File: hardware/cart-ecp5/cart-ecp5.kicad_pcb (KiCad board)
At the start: 4 copper layers, 100 x 60 mm, 129 parts, among them J1 JTAG, J2 MicroSD_Molex_1040310811, J3 N64_Cartridge_Bus, J5 USB_C_USB2.0, U1 LFE5U-25F-xBG256x, U10 93C46BT-I_OT, U11 FT2232HQ, U13 TLV62568DBV, U2 W25Q512JVEIM, U3 S27KS0641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

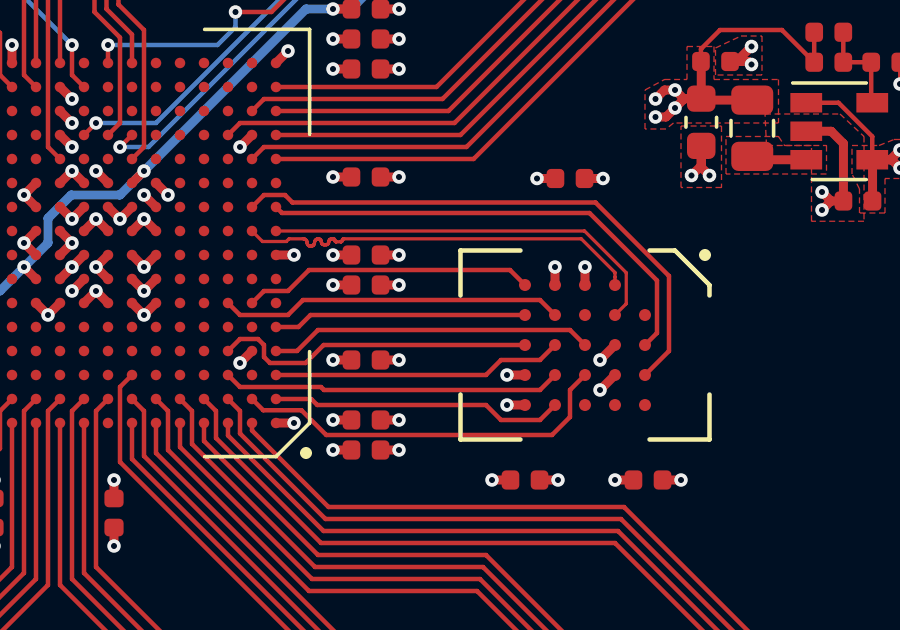
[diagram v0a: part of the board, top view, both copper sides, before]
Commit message: First pass at length matching HyperRAM interface
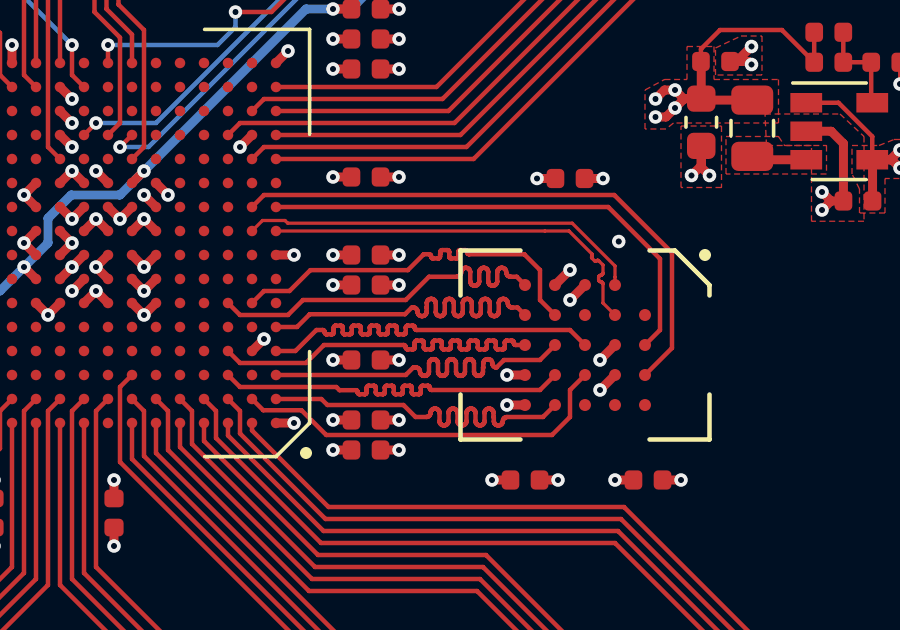
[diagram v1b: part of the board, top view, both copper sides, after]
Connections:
- U1 pad F2: HRAM_DQ7 -> HRAM_DQ1
- U1 pad F3: HRAM_DQ1 -> HRAM_DQ7
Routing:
- net HRAM_DQ6: track 8.47 -> 13.1 mm
- net HRAM_DQ0: track 9.71 -> 13.1 mm
- net HRAM_DQ4: track 9.80 -> 13.1 mm
- net HRAM_DQ7: track 9.76 -> 12.9 mm
- net HRAM_RWDS: track 10.8 -> 13.0 mm
- net HRAM_DQ5: track 10.9 -> 13.0 mm
- net HRAM_DQ3: track 11.3 -> 13.0 mm
- net HRAM_DQ1: track 11.5 -> 13.0 mm
- net HRAM_RESET_B: track 18.8 -> 19.4 mm
- net HRAM_CS_B: track 16.0 -> 16.6 mm
- net GND: track 187.9 -> 188.0 mm, vias 108 -> 109

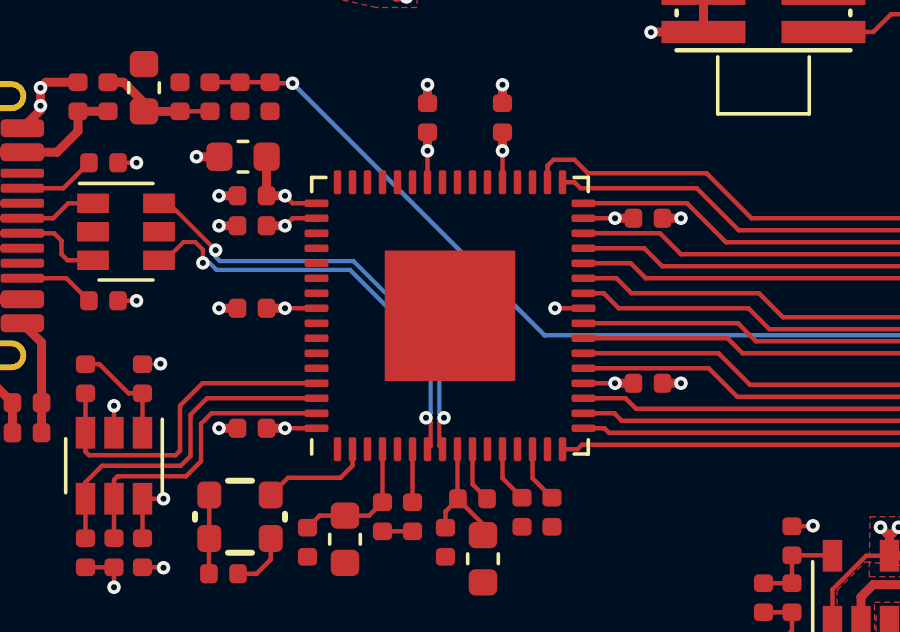
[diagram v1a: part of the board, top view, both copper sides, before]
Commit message: Adjust the P1V8 power plane to insect the switcher output
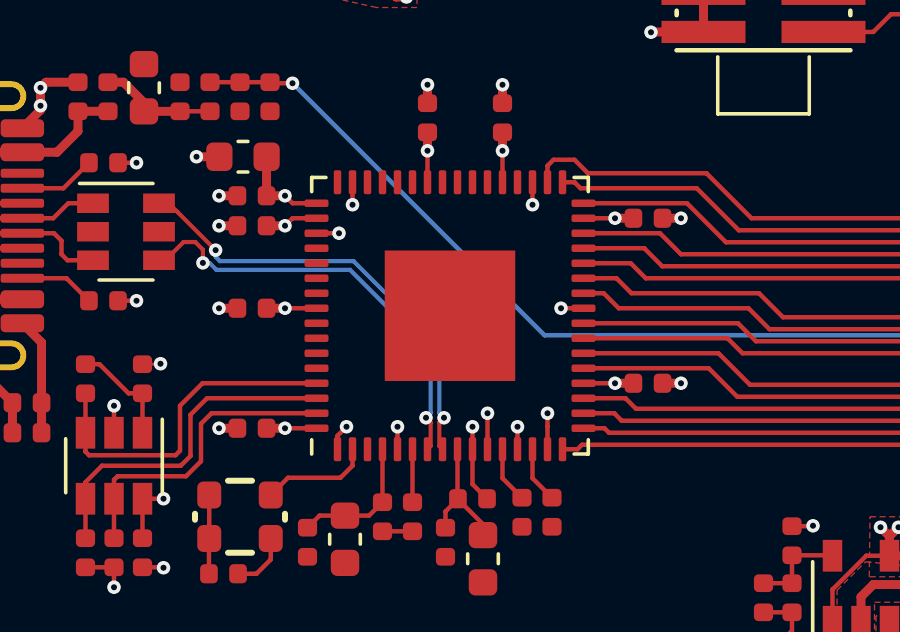
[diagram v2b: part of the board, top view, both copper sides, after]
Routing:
- net GND: track 188.0 -> 195.6 mm, vias 109 -> 118

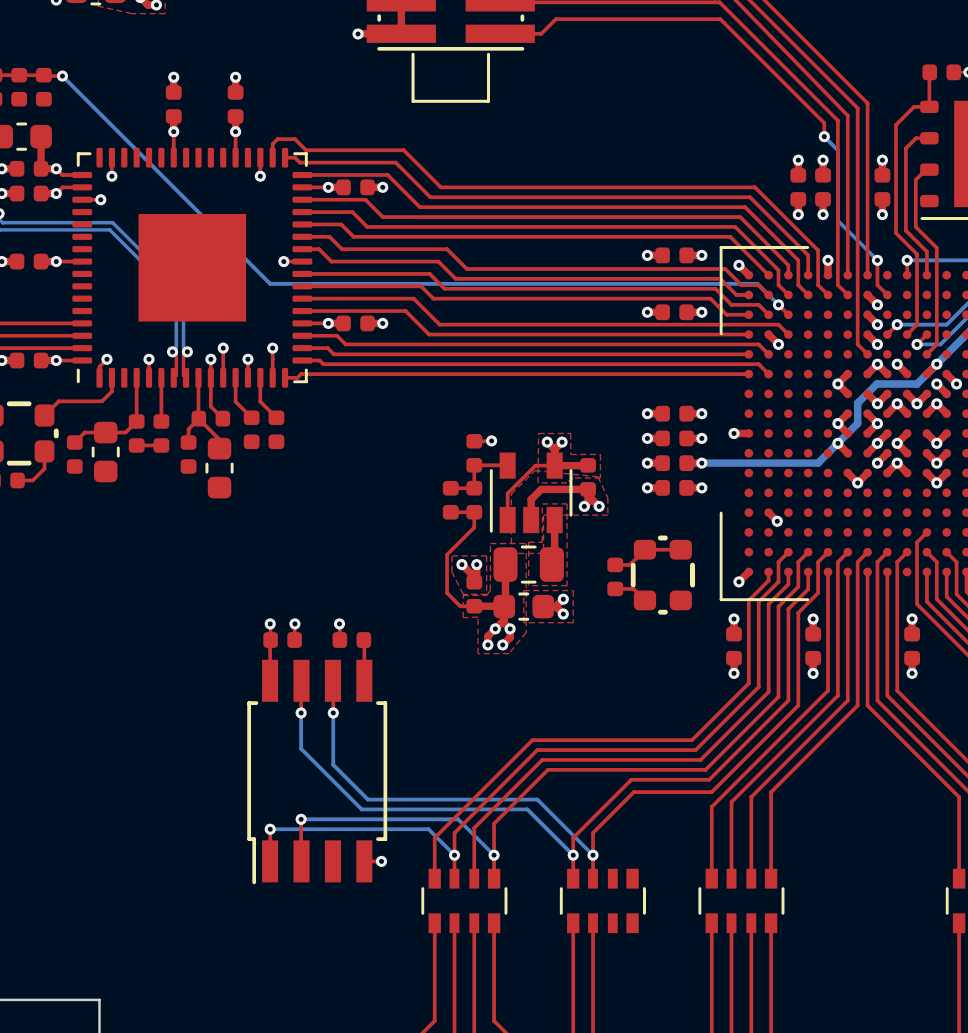
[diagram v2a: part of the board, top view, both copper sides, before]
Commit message: Add more clearance to FT2232H interface to study length matching
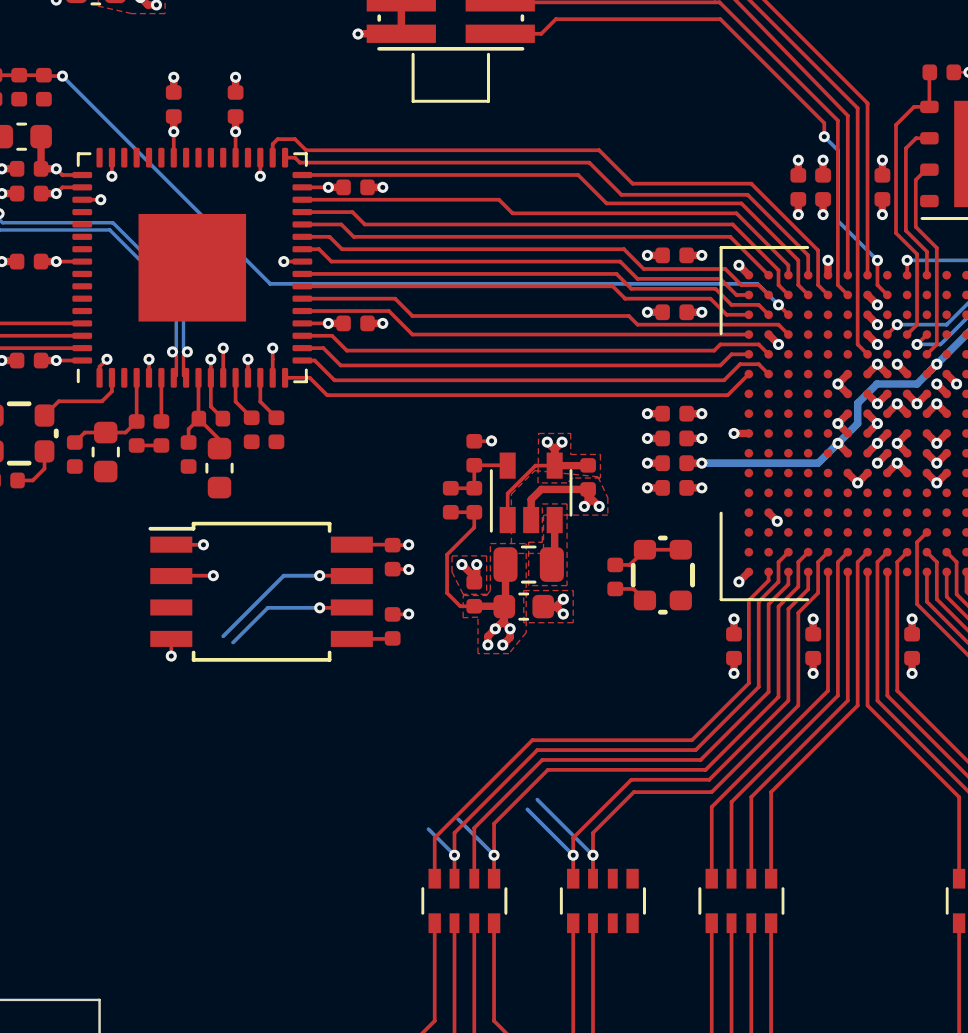
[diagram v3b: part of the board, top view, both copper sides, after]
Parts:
- moved U4 7.59 mm to (124.3, 107.0), turned to 0 degrees
- moved C41 5.57 mm to (129.6, 105.6), turned to 270 degrees
- moved R6 1.74 mm to (129.6, 108.4), turned to 270 degrees
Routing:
- net N64_CIC_DATA2: track 34.4 -> 27.5 mm
- net N64_CIC_DATA1: track 33.7 -> 27.0 mm
- net N64_COLD_RESET#: track 31.7 -> 25.3 mm
- net N64_S_CLK: track 32.3 -> 26.0 mm
- net USB_AD0: track 18.8 -> 19.4 mm
- net USB_AD1: track 19.1 -> 19.6 mm

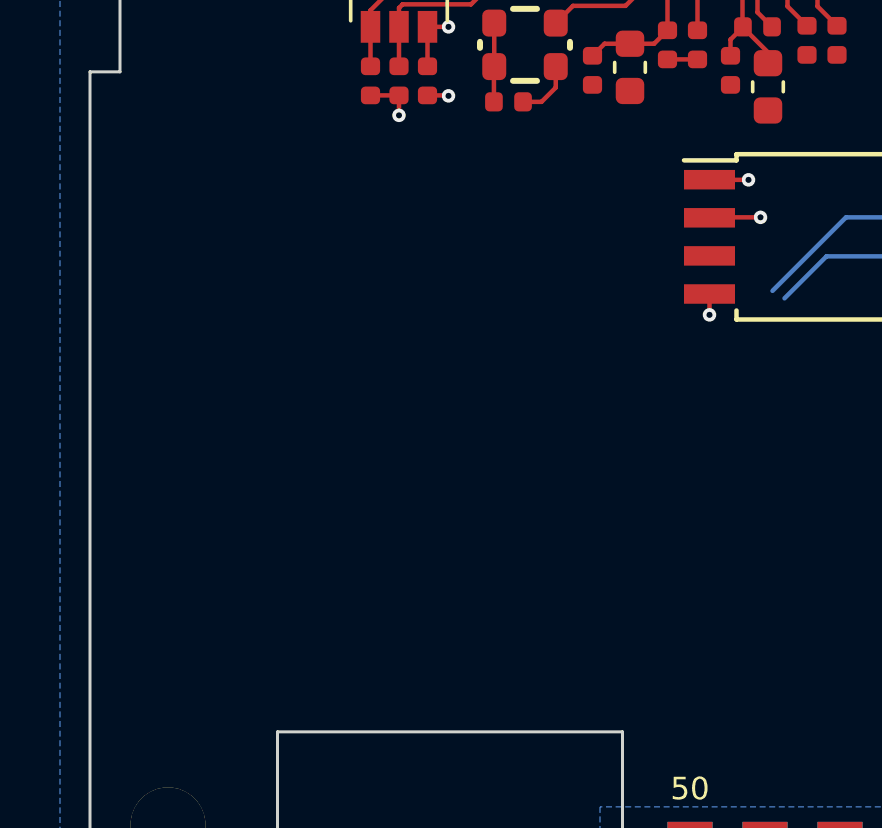
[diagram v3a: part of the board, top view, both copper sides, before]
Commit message: Add debugging LEDs with preliminary layout
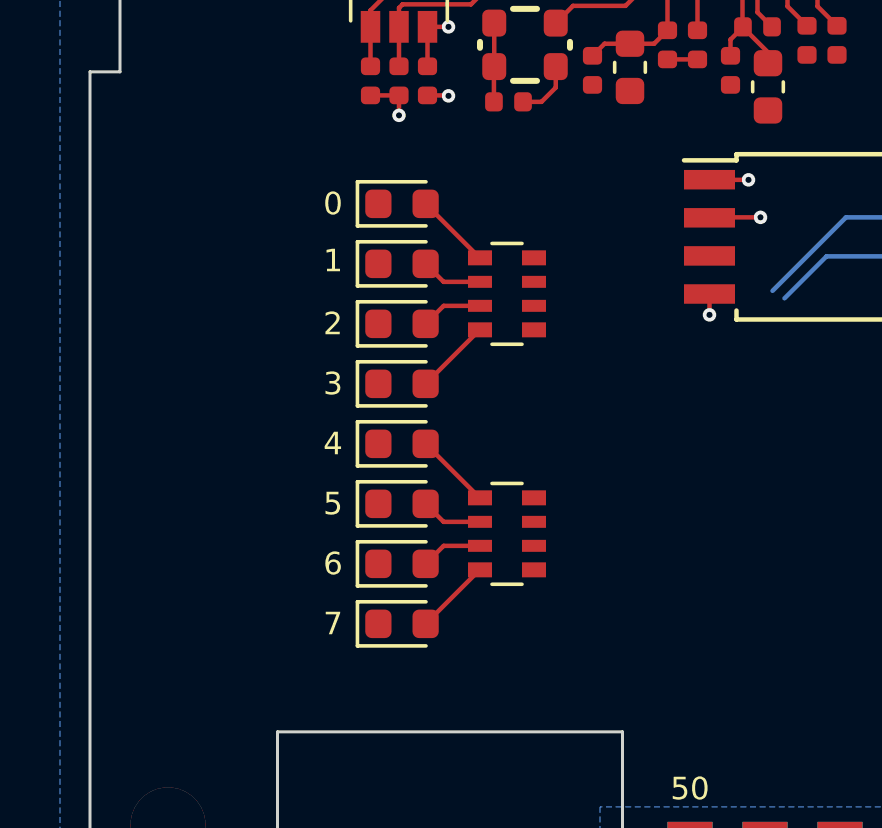
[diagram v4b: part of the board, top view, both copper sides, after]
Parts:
- added D1: LED, Diode_SMD:D_0603_1608Metric, F.Cu at (110.4, 105.9)
- added D2: LED, Diode_SMD:D_0603_1608Metric, F.Cu at (110.4, 107.9)
- added D3: LED, Diode_SMD:D_0603_1608Metric, F.Cu at (110.4, 109.9)
- added D4: LED, Diode_SMD:D_0603_1608Metric, F.Cu at (110.4, 111.9)
- added D5: LED, Diode_SMD:D_0603_1608Metric, F.Cu at (110.4, 113.9)
- added D6: LED, Diode_SMD:D_0603_1608Metric, F.Cu at (110.4, 115.9)
- added D7: LED, Diode_SMD:D_0603_1608Metric, F.Cu at (110.4, 117.9)
- added D8: LED, Diode_SMD:D_0603_1608Metric, F.Cu at (110.4, 119.9)
- added RN10: 200R, Resistor_SMD:R_Array_Convex_4x0603, F.Cu at (113.9, 116.9)
- added RN9: 200R, Resistor_SMD:R_Array_Convex_4x0603, F.Cu at (113.9, 108.9)
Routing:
- net Net-(D8-Pad2): track 0.00 -> 2.56 mm
- net Net-(D4-Pad2): track 0.00 -> 2.56 mm
- net Net-(D5-Pad2): track 0.00 -> 2.56 mm
- net Net-(D1-Pad2): track 0.00 -> 2.56 mm
- net Net-(D7-Pad2): track 0.00 -> 2.06 mm
- net Net-(D3-Pad2): track 0.00 -> 2.06 mm
- net Net-(D6-Pad2): track 0.00 -> 2.06 mm
- net Net-(D2-Pad2): track 0.00 -> 2.06 mm
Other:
- board text added: "0"
- board text added: "2"
- board text added: "3"
- board text added: "4"
- board text added: "5"
- board text added: "6"
- board text added: "7"

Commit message: Finish adding copper zones to the power mux
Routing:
- net GND: track 195.6 -> 196.0 mm, vias 118 -> 119

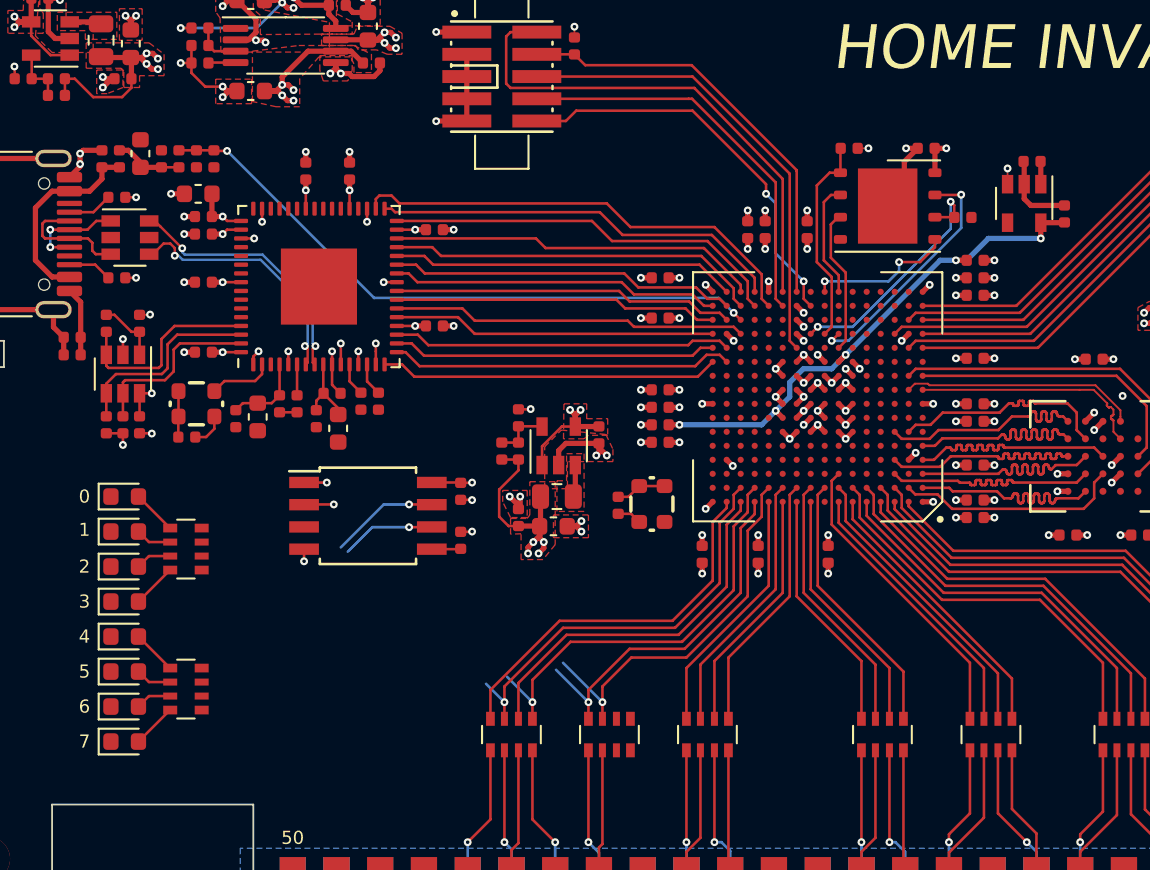
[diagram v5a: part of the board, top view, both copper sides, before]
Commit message: More power layout for USB interface
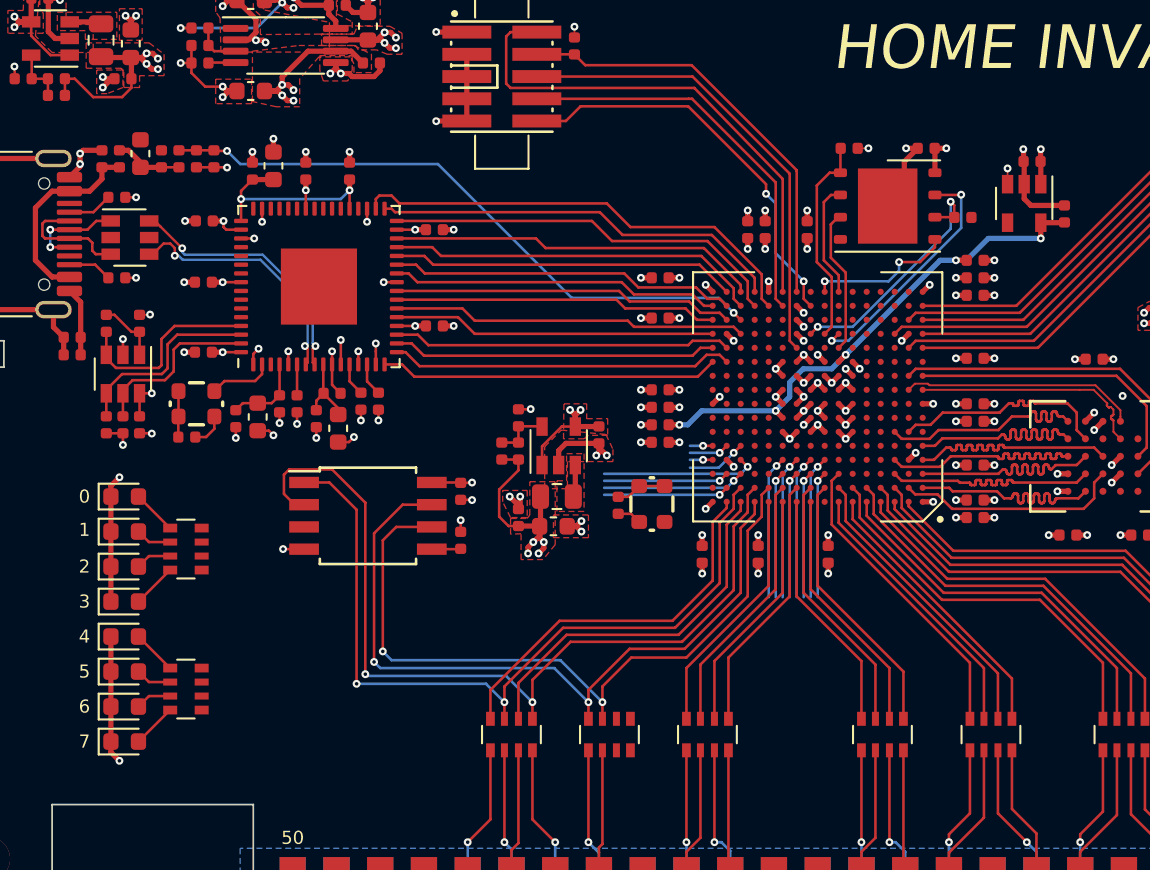
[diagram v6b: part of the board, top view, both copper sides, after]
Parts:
- moved C38 4.59 mm to (118.9, 87.0), turned to 90 degrees
- moved C39 3.82 mm to (117.7, 87.3), turned to 90 degrees
- moved C40 0.75 mm to (115.0, 90.2)
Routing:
- net N64_S_CLK: track 26.0 -> 50.3 mm
- net GND: track 196.0 -> 216.9 mm, vias 119 -> 128
- net N64_COLD_RESET#: track 25.3 -> 45.0 mm
- net N64_CIC_DATA1: track 27.0 -> 42.7 mm
- net N64_CIC_DATA2: track 27.5 -> 42.2 mm
- net Net-(U1-PadD14): track 0.00 -> 8.93 mm, vias 0 -> 1
- net Net-(U1-PadD8): track 0.00 -> 8.18 mm, vias 0 -> 1
- net Net-(U1-PadD11): track 0.00 -> 8.18 mm, vias 0 -> 1
- net Net-(U1-PadD10): track 0.00 -> 8.18 mm, vias 0 -> 1
- net Net-(U1-PadD9): track 0.00 -> 8.18 mm, vias 0 -> 1
- net Net-(U1-PadC14): track 0.00 -> 8.13 mm, vias 0 -> 1
- net Net-(U1-PadC9): track 0.00 -> 7.22 mm, vias 0 -> 1
- net Net-(U1-PadC8): track 0.00 -> 7.22 mm, vias 0 -> 1
- net Net-(U1-PadC11): track 0.00 -> 7.22 mm, vias 0 -> 1
- net Net-(U1-PadC10): track 0.00 -> 7.22 mm, vias 0 -> 1
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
